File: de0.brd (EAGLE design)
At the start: 150.7 x 90.7 mm, 137 parts, among them IC1 PL2303SA__LF, J1 JUMPER_IN_50, J2 UX60SC-MB-5ST, J3 REG_OUT_33, U1 P0082, U2 RFM95W-915S2, U3 TPS76201DBVR, U4 TPS76201DBVR, U5 TPS76201DBVR

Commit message: Update layout again
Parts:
- moved JP1 2.10 mm to (-59.5, 35.9)
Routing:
- net JTAG_TDO: track 44.5 -> 42.4 mm
- net JTAG_TDI: track 36.8 -> 34.7 mm
- net JTAG_TCK: track 40.5 -> 38.4 mm
- net JTAG_TMS: track 38.6 -> 36.7 mm
- net ADDRESS_11: track 61.5 -> 59.6 mm
- net VDD: track 88.4 -> 90.1 mm
- net GND: track 295.4 -> 296.3 mm
- net VDDLS: track 86.6 -> 85.8 mm
- added copper zone on layer 1, net VDD
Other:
- board size 150.7 x 90.7 mm -> 149.9 x 88.9 mm

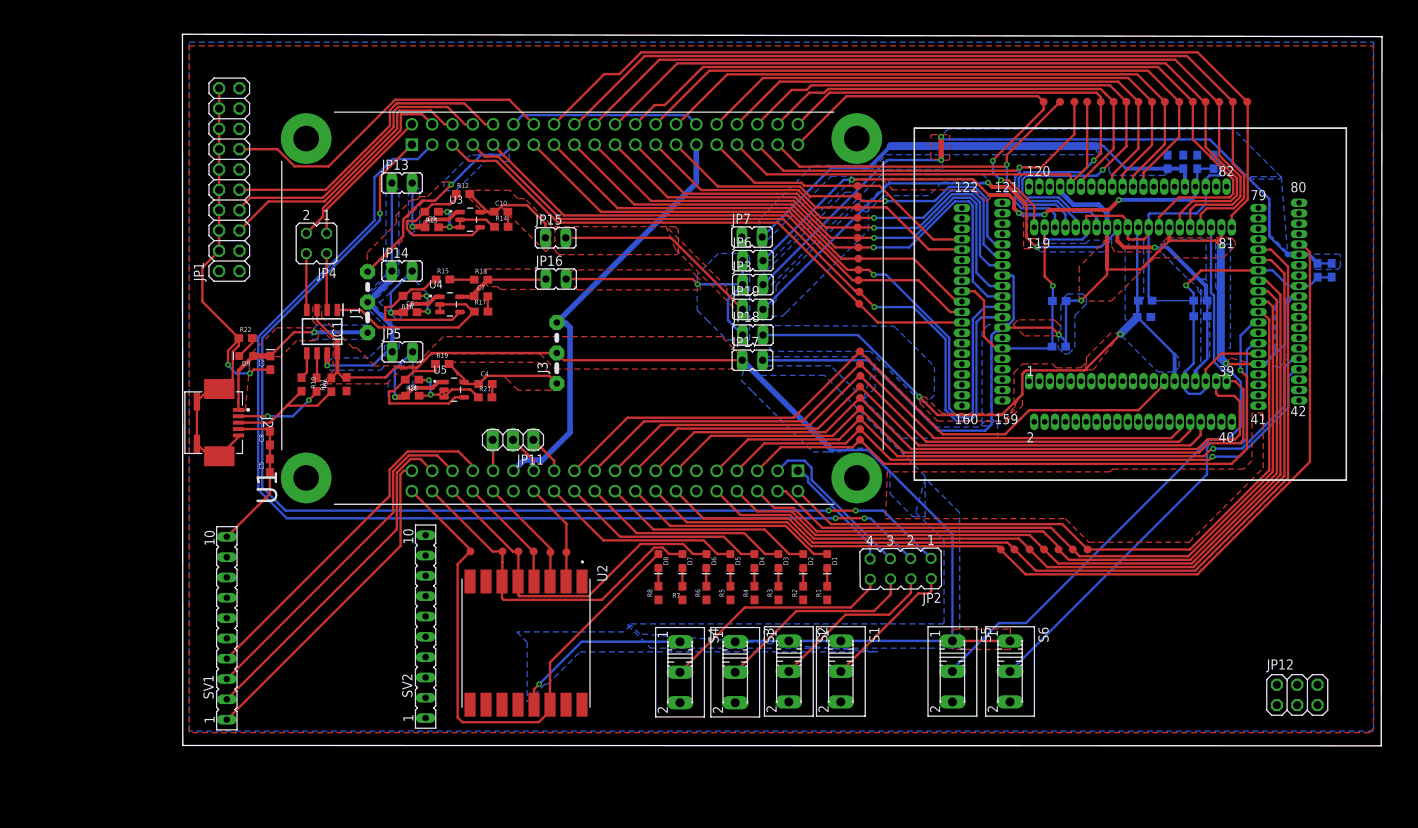
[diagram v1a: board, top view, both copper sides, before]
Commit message: Add more via for power connection
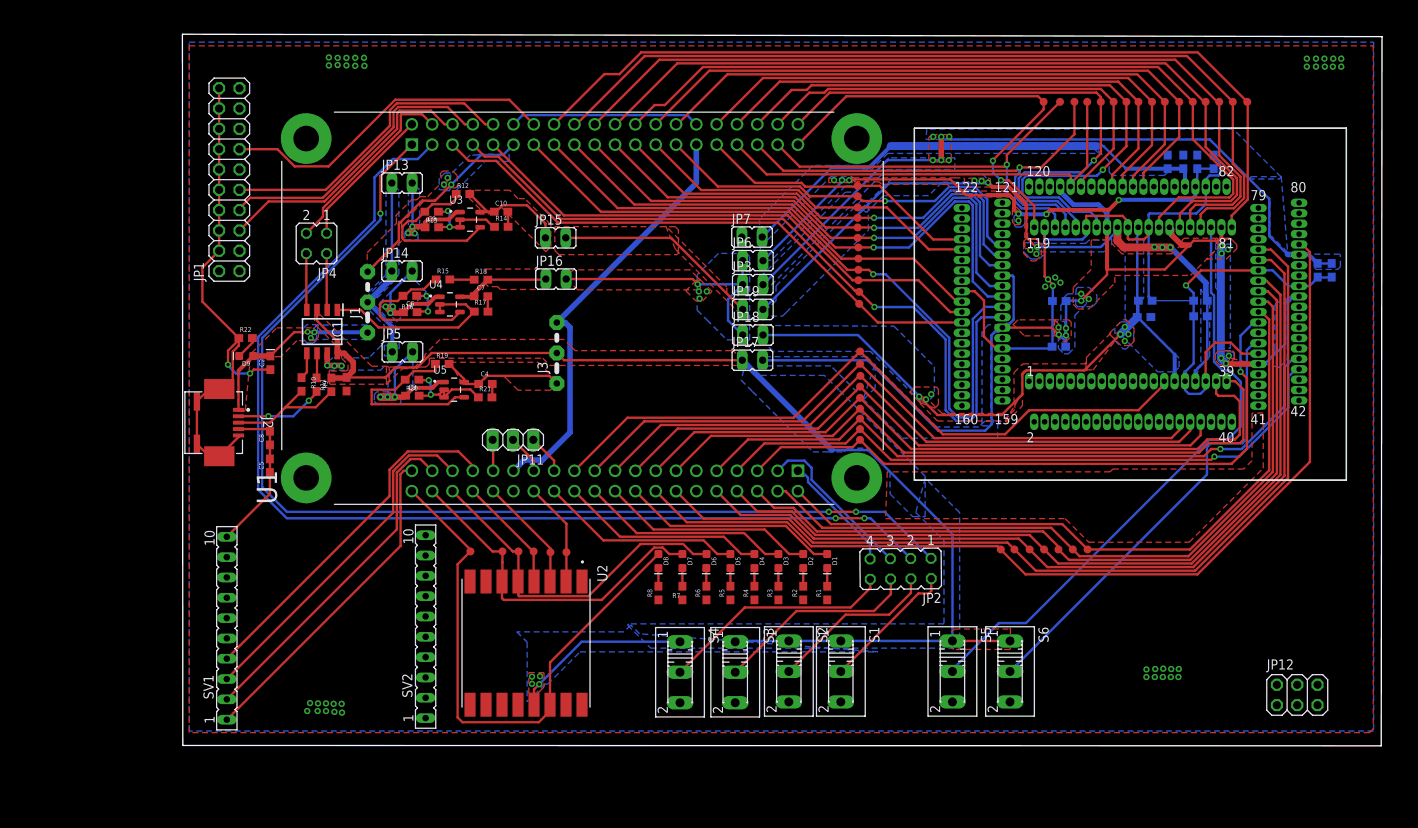
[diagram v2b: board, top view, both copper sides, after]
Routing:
- net VDD5: track 34.0 -> 27.0 mm, vias 1 -> 3
- net N$34: track 18.9 -> 23.6 mm
- net VDDLS: track 85.8 -> 89.1 mm, vias 3 -> 9
- net IN_12: track 13.3 -> 16.3 mm, vias 1 -> 3
- net IN_07: track 12.6 -> 15.5 mm, vias 1 -> 3
- net GND: track 296.3 -> 298.9 mm, vias 10 -> 54
- net VCCQ: track 140.8 -> 142.9 mm, vias 4 -> 13
- net N$29: track 18.8 -> 20.7 mm
- net IN_33: track 13.5 -> 15.3 mm, vias 1 -> 3
- net VO_33: track 168.1 -> 169.8 mm, vias 1 -> 4
- net N$30: track 19.1 -> 20.4 mm
- net VBP: track 67.5 -> 67.4 mm, vias 4 -> 7
- net GPIO0_VCC_5V: vias 1 -> 3
- net VO_12: vias 1 -> 4
- net VDDH: vias 2 -> 7
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
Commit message: Organize the schematic and the layout
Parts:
- removed C5, C8: 1nF, SparkFun-Capacitors:0603
- removed JP15: REG_OUT_07, jumper:JP1
- removed JP16: REG_OUT_12, jumper:JP1
- removed JP17: VCCQ, jumper:JP1
- removed JP18: VDDH, jumper:JP1
- removed JP19: VDDLS, jumper:JP1
- removed JP2: SWITCH, jumper:JP4Q
- removed JP3: VDD, jumper:JP1
- removed JP5: REG_IN_33, jumper:JP1
- removed JP6: VBP, jumper:JP1
- removed JP7: VBN, jumper:JP1
- removed U$16: INTERRUPTS_6, qfp160:POINT
- added INTERRUPTS_6: INTERRUPTS_6, qfp160:POINT
- added REG_IN_33: REG_IN_33, jumper:JP1
- added REG_OUT_07: REG_OUT_07, jumper:JP1
- added REG_OUT_12: REG_OUT_12, jumper:JP1
- added SWITCH: SWITCH, jumper:JP4Q
- added VBN: VBN, jumper:JP1
- added VBP: VBP, jumper:JP1
- added VCCQ: VCCQ, jumper:JP1
- added VDD: VDD, jumper:JP1
- added VDDH: VDDH, jumper:JP1
- added VDDLS: VDDLS, jumper:JP1
- moved D1 4.98 mm to (14.7, -16.8)
- moved D2 4.98 mm to (11.7, -16.8)
- moved D3 4.98 mm to (8.55, -16.8)
- moved D4 4.98 mm to (5.55, -16.8)
- moved D5 4.98 mm to (2.55, -16.8)
- moved D7 4.97 mm to (-3.35, -16.8)
- moved D6 4.96 mm to (-0.25, -16.8)
- moved D8 4.96 mm to (-6.15, -16.8)
- moved C12 4.14 mm to (44.2, 19.1)
- moved R4 2.41 mm to (5.55, -13.4)
- moved R5 2.41 mm to (2.55, -13.4)
- moved R1 2.41 mm to (14.7, -13.4)
- moved R2 2.41 mm to (11.7, -13.4)
- moved R3 2.41 mm to (8.55, -13.4)
- moved R7 2.39 mm to (-3.35, -13.4)
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- renumbered J1 to 5V_JUMPER, J3 to REG_OUT_33, JP1 to JTAG, JP11 to PIN_OUT, JP13 to REG_IN_07, JP14 to REG_IN_12, JP4 to UART_JUMPER, S5 to RESET, S6 to LOCKED
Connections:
- net N$18 renamed D-
- net N$19 renamed D+
- removed net N$13: JP2.2, S1.2
- removed net N$14: JP2.4, S2.2
- removed net N$15: JP2.6, S3.2
- removed net N$16: JP2.8, S4.2
- removed net N$24: JP2.5, U1.JP2_3
- new net GPIO0_IN_0: SWITCH.1, U1.JP1_1
- new net GPIO0_IN_1: SWITCH.3, U1.JP1_3
- new net GPIO1_IN_0: SWITCH.7, U1.JP2_1
- new net GPIO1_IN_1: SWITCH.5, U1.JP2_3
- new net N$12: S1.2, SWITCH.2
- net GND: now also D1.C, D2.C, D3.C, D4.C, D5.C, D6.C, D7.C, D8.C, VBN.1; no longer C5.1, C5.2, C8.1, C8.2, JP7.1, R1.1, R2.1, R3.1, R4.1, R5.1, R6.1, R7.1, R8.1
- net GPIO_OUT_0: now also R1.2; no longer D1.A
- net GPIO_OUT_1: now also R2.2; no longer D2.A
- net GPIO_OUT_2: now also R3.2; no longer D3.A
- net GPIO_OUT_3: now also R4.2; no longer D4.A
- net GPIO_OUT_4: now also R5.2; no longer D5.A
- net INTERRUPTS_6: now also INTERRUPTS_6.1; no longer U$16.1
- net IN_33: now also REG_IN_33.2; no longer JP5.2
- net LORA_DIO0: now also R8.2; no longer D8.A
- net LORA_NSS: now also R6.2; no longer D6.A
- net LORA_RESET: now also R7.2; no longer D7.A
- net N$1: now also D1.A, R1.1; no longer D1.C, R1.2
- net N$10: now also S3.2, SWITCH.6; no longer JP2.3, U1.JP1_3
- net N$11: now also S2.2, SWITCH.4; no longer JP2.7, U1.JP2_1
- net N$2: now also D8.A, R8.1; no longer D2.C, R2.2
- net N$3: now also D7.A, R7.1; no longer D3.C, R3.2
- net N$4: now also D6.A, R6.1; no longer D4.C, R4.2
- net N$5: now also D5.A, R5.1; no longer D5.C, R5.2
- net N$6: now also D4.A, R4.1; no longer D6.C, R6.2
- net N$7: now also D2.A, R2.1; no longer D7.C, R7.2
- net N$8: now also D3.A, R3.1; no longer D8.C, R8.2
- net N$9: now also S4.2, SWITCH.8; no longer JP2.1, U1.JP1_1
- net OUT_07: now also REG_OUT_07.1; no longer JP15.1
- net OUT_12: now also REG_OUT_12.1; no longer JP16.1
- net VBN: now also VBN.2; no longer JP7.2
- net VBP: now also VBP.2; no longer JP6.2
- net VCCQ: now also VCCQ.2; no longer JP17.2
- net VDD: now also VDD.2; no longer JP3.2
- net VDD5: now also REG_IN_33.1; no longer JP5.1
- net VDDH: now also VDDH.2; no longer JP18.2
- net VDDLS: now also VDDLS.2; no longer JP19.2
- net VO_07: now also REG_OUT_07.2, VDDLS.1; no longer JP15.2, JP19.1
- net VO_12: now also REG_OUT_12.2, VBP.1, VDD.1, VDDH.1; no longer JP16.2, JP18.1, JP3.1, JP6.1
- net VO_33: now also VCCQ.1; no longer JP17.1
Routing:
- net GPIO0_IN_1: track 0.00 -> 143.2 mm, vias 0 -> 2
- net GPIO0_IN_0: track 0.00 -> 141.1 mm, vias 0 -> 3
- net N$10: track 139.1 -> 22.3 mm, vias 2 -> 0
- net N$9: track 137.9 -> 24.7 mm, vias 3 -> 0
- net GND: track 298.9 -> 214.2 mm, vias 54 -> 45
- net N$16: track 29.2 -> 0.00 mm
- net N$15: track 25.4 -> 0.00 mm
- net INTERRUPTS_4: track 108.9 -> 134.0 mm, vias 0 -> 2
- net GPIO1_IN_1: track 0.00 -> 22.1 mm
- net N$14: track 21.1 -> 0.00 mm
- net N$24: track 20.6 -> 0.00 mm
- net INTERRUPTS_5: track 116.4 -> 136.9 mm, vias 0 -> 2
- net N$13: track 17.0 -> 0.00 mm
- net GPIO1_IN_0: track 0.00 -> 16.1 mm
- net WR_DATA_3: track 71.7 -> 87.6 mm
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- added copper zone on layer 1, net IN_07
- added copper zone on layer 1, net IN_12
- added copper zone on layer 1, net IN_33
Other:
- board size 149.9 x 88.9 mm -> 150.2 x 88.8 mm
- board text added: "3.3V_GPIO"
- board text added: "3.3V_REG"
- board text added: "5V_GPIO"
- board text added: "5V_USB"
- board text added: "ADDRESS_0"
- board text added: "ADDRESS_1"
- board text added: "ADDRESS_10"
- board text added: "ADDRESS_11"
- board text added: "ADDRESS_12"
- board text added: "ADDRESS_13"
- board text added: "ADDRESS_14"
- board text added: "ADDRESS_15"
- board text added: "ADDRESS_2"
- board text added: "ADDRESS_3"
- board text added: "ADDRESS_4"
- board text added: "ADDRESS_5"
- board text added: "ADDRESS_6"
- board text added: "ADDRESS_7"
- board text added: "ADDRESS_8"
- board text added: "ADDRESS_9"
- board text added: "CLOCK"
- board text added: "INTERRUPTS_0"
- board text added: "INTERRUPTS_1"
- board text added: "INTERRUPTS_2"
- board text added: "INTERRUPTS_3"
- board text added: "INTERRUPTS_4"
- board text added: "INTERRUPTS_5"
- board text added: "INTERRUPTS_6"
- board text added: "INTERRUPTS_7"
- board text added: "JTAG_TDI"
- board text added: "JTAG_TDO"
- board text added: "JTAG_TMS"
- board text added: "LORA_DIO0"
- board text added: "LORA_MISO"
- board text added: "LORA_MOSI"
- board text added: "LORA_NSS"
- board text added: "LORA_RESET"
- board text added: "LORA_SCK"
- board text added: "RD_DATA_0"
- board text added: "RD_DATA_1"
- board text added: "RD_DATA_2"
- board text added: "RD_DATA_3"
- board text added: "RD_DATA_4"
- board text added: "RD_DATA_5"
- board text added: "RD_DATA_6"
- board text added: "RD_DATA_7"
- board text added: "RD_EN"
- board text added: "USEC_TICK"
- board text added: "WR_DATA_0"
- board text added: "WR_DATA_1"
- board text added: "WR_DATA_2"
- board text added: "WR_DATA_3"
- board text added: "WR_DATA_4"
- board text added: "WR_DATA_5"
- board text added: "WR_DATA_6"
- board text added: "WR_DATA_7"
- board text added: "WR_EN"

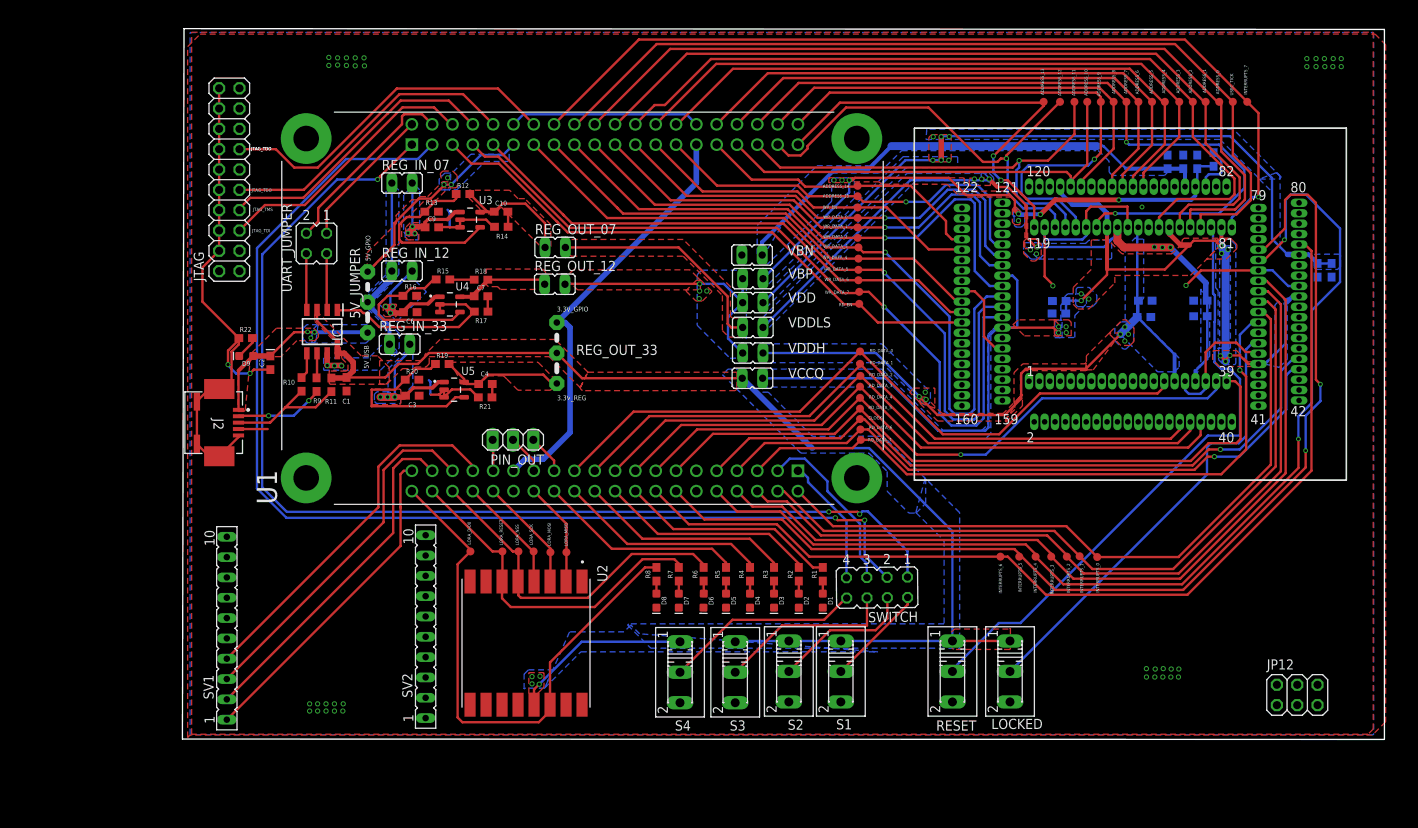
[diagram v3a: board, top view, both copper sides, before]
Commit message: Add 4 holes for the screws
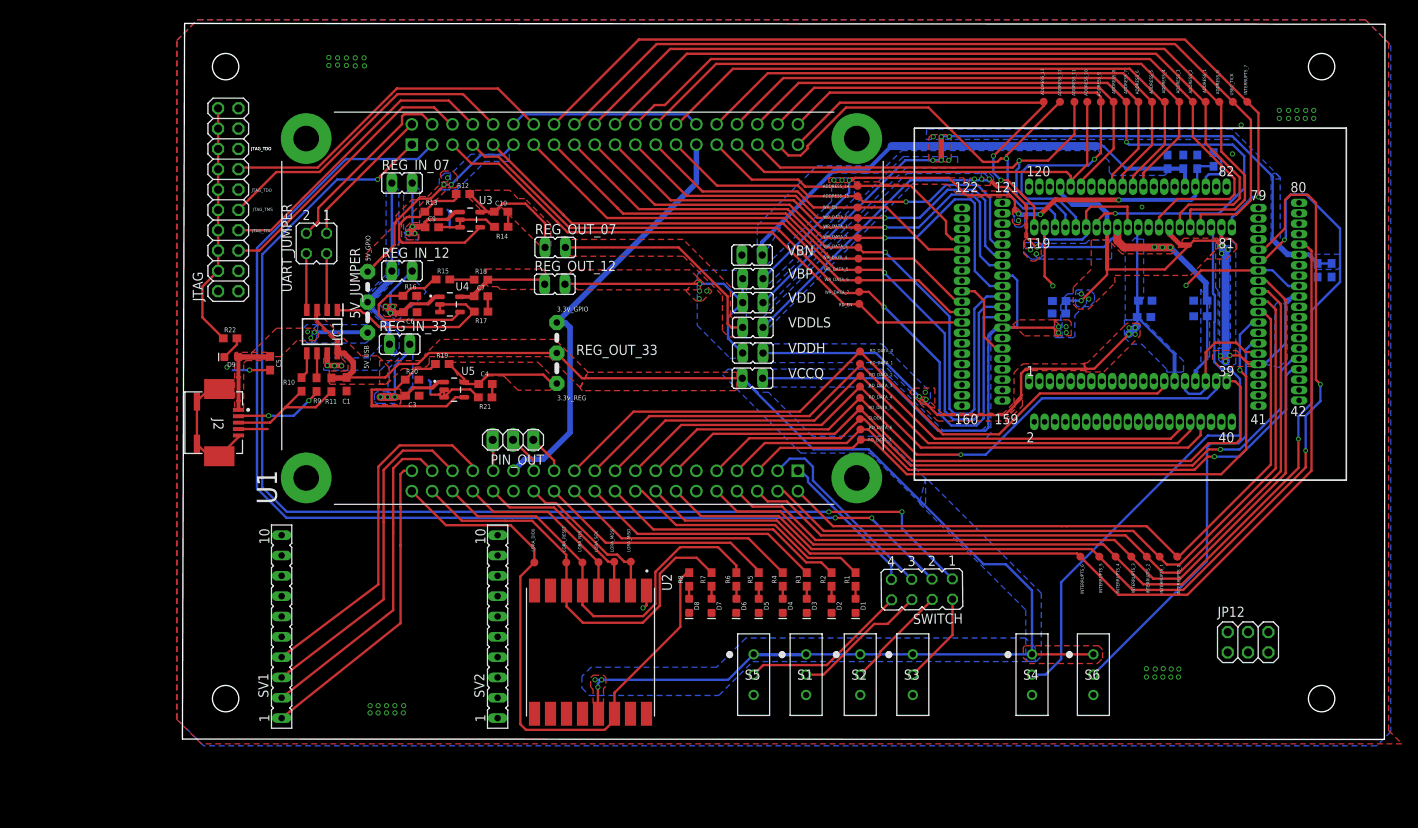
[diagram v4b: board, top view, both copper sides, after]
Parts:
- removed C2: 10uF, SparkFun-Capacitors:0603-POLAR
- removed LOCKED: LOCKED, switch:255SB
- removed RESET: RESET, switch:255SB
- added C5: 10uF, SparkFun-Capacitors:0603
- added S5, S6: SS12SDP2, SamacSys_Parts:SS12SDP2
- S1: value SWITCH0 -> SS12SDP2; device switch:255SB -> SamacSys_Parts:SS12SDP2
- S2: value SWITCH -> SS12SDP2; device switch:255SB -> SamacSys_Parts:SS12SDP2
- S3: value SWITCH2 -> SS12SDP2; device switch:255SB -> SamacSys_Parts:SS12SDP2
- S4: value SWITCH3 -> SS12SDP2; device switch:255SB -> SamacSys_Parts:SS12SDP2
- moved S4 44.0 mm to (40.8, -26.0), turned to 0 degrees
- moved S3 22.2 mm to (25.9, -26.0), turned to 0 degrees
- moved U$10 10.0 mm to (59.0, -11.2)
- moved U$11 10.0 mm to (56.8, -11.2)
- moved INTERRUPTS_6 10.0 mm to (46.9, -11.2)
- moved U$12 10.0 mm to (55.1, -11.2)
- moved U$13 10.0 mm to (53.2, -11.2)
- moved U$14 10.0 mm to (51.2, -11.2)
- moved U$15 10.0 mm to (49.2, -11.2)
- moved JP12 9.01 mm to (67.8, -21.9)
- moved SV2 9.00 mm to (-26.0, -20.0)
- moved S2 8.94 mm to (19.3, -26.0), turned to 0 degrees
- moved U$50 8.22 mm to (-13.4, -11.9)
- moved U2 8.14 mm to (-14.4, -23.2)
- moved U$48 8.14 mm to (-9.35, -11.9)
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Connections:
- net N$11 renamed GPIO_1
- removed net N$10: S3.2, SWITCH.6
- removed net N$12: S1.2, SWITCH.2
- removed net N$9: S4.2, SWITCH.8
- new net GPIO_0: S3.2, SWITCH.2
- new net GPIO_2: S1.2, SWITCH.6
- new net GPIO_3: S5.2, SWITCH.8
- net GND: now also C5.2, S5.3, S6.3; no longer C2.-, LOCKED.3, RESET.3
- net LOCKED: now also S6.2; no longer LOCKED.2
- net RESET: now also S4.2; no longer RESET.2
- net VDD5_USB: now also C5.1; no longer C2.+
- net VO_33: now also S5.1, S6.1; no longer LOCKED.1, RESET.1
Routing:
- net VO_33: track 170.0 -> 195.1 mm, vias 4 -> 3
- net N$9: track 24.7 -> 0.00 mm
- net N$10: track 22.3 -> 0.00 mm
- net GPIO_3: track 0.00 -> 21.2 mm
- net GPIO_2: track 0.00 -> 17.1 mm
- net N$12: track 12.7 -> 0.00 mm
- net GND: track 214.2 -> 202.4 mm, vias 45 -> 48
- net GPIO_0: track 0.00 -> 11.5 mm
- net LORA_NSS: track 43.5 -> 52.8 mm
- net LORA_RESET: track 43.5 -> 52.0 mm
- net LORA_SCK: track 14.5 -> 22.9 mm
- net LORA_MOSI: track 14.6 -> 22.4 mm
- net LORA_DIO0: track 68.7 -> 76.0 mm
- net LORA_MISO: track 13.3 -> 19.4 mm
- net VDD5_USB: track 23.0 -> 17.3 mm
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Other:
- board size 150.2 x 88.8 mm -> 150.3 x 89.5 mm

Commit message: Update again schematic  for consistency
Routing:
- net GND: vias 48 -> 47
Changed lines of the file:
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@@
 <via x="-57" y="12.07" extent="1-16" drill="0.4"/>
 <wire x1="-57" y1="12.07" x2="-59.12" y2="12.07" width="0.3" layer="16"/>
-<via x="-59.83" y="12.44" extent="1-16" drill="0.4"/>
 <via x="55.1" y="-26.3" extent="1-16" drill="0.4"/>
 <via x="56.15" y="-26.3" extent="1-16" drill="0.4"/>
